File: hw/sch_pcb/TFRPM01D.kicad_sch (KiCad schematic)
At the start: 22 parts, among them J1 HEADER_1x03, J2 SM04B-GHS-TB, J3 SM04B-GHS-TB, M2 M3, U1 PCF8583, U2 SN74LVC1G14-Q1, U3 MIC5504-3.3YM5

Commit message: update action, clean repo
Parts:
- added D3: LED GREEN, LED_SMD:LED_1206_3216Metric_ReverseMount_Hole1.8x2.4mm, symbol Device:LED
- added R5: R, Resistor_SMD:R_0603_1608Metric, symbol Device:R
- C1, C4, C5, C6: footprint Mlab_R:SMD-0603 -> Capacitor_SMD:C_0603_1608Metric
- C2, C3: footprint Mlab_R:SMD-0805 -> Capacitor_SMD:C_0805_2012Metric
- D1: footprint Mlab_D:Diode-MiniMELF_Standard -> Diode_SMD:D_MiniMELF
- D2: footprint Mlab_D:LED_1206 -> LED_SMD:LED_1206_3216Metric_ReverseMount_Hole1.8x2.4mm
- R1, R2: footprint Mlab_R:SMD-0805 -> Resistor_SMD:R_0805_2012Metric
- R10, R3, R4: footprint Mlab_R:SMD-0603 -> Resistor_SMD:R_0603_1608Metric
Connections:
- net +5V: now also D3.2 (A)
- net GND: now also R5.2
- new net: D3.1 (K), R5.1

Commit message: procisteni dat
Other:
- title: TFRPM01C -> TFRPM01D
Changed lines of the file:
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@@
   (paper "A4")
   (title_block
-    (title "TFRPM01C")
-    (date "2021-04-05")
+    (title "TFRPM01D")
+    (date "2022-03-29")
     (company "ThunderFly s.r.o.")
     (comment 1 "RPM measuring device for UAVs")
     (comment 2 "Jacho  <info@thunderfly.cz>")
+    (comment 3 "roman-dvorak")
   )
   (junction (at 165.1 111.76) (diameter 1.016) (color 0 0 0 0)

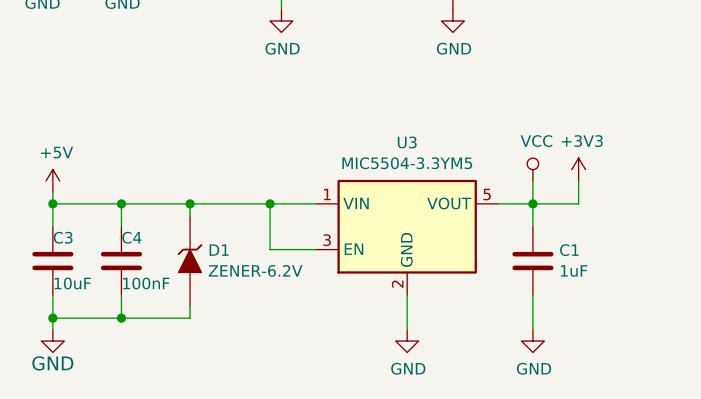
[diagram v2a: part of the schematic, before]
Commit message: Výměna pouzder LED a D zener
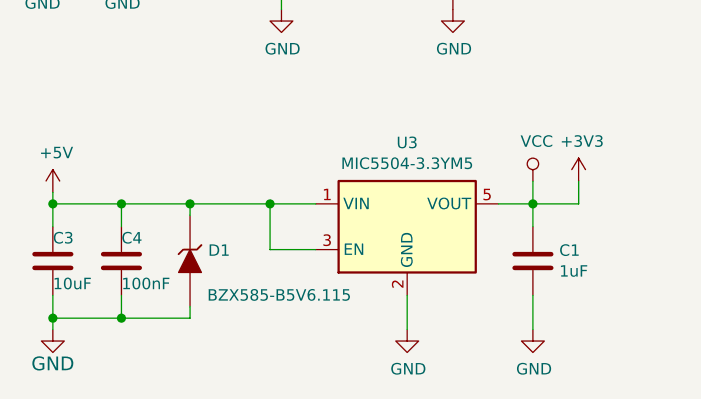
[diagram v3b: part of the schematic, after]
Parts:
- D1: value ZENER-6.2V -> BZX585-B5V6.115; footprint Diode_SMD:D_MiniMELF -> Diode_SMD:D_SOD-523; UST_ID 604b0326128750769e5b0f93 -> 60879d38128750769ee58e48
- D2, D3: footprint LED_SMD:LED_1206_3216Metric_ReverseMount_Hole1.8x2.4mm -> Mlab_D:LED_1206
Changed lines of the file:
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@@
       (effects (font (size 1.27 1.27)) (justify left))
     )
-    (property "Value" "ZENER-6.2V" (id 1) (at 45.187 176.403 90)
-      (effects (font (size 1.27 1.27)) (justify left))
-    )
-    (property "Footprint" "Diode_SMD:D_MiniMELF" (id 2) (at 43.18 175.26 0)
+    (property "Value" "BZX585-B5V6.115" (id 1) (at 45.085 179.07 90)
+      (effects (font (size 1.27 1.27)) (justify left))
+    )
+    (property "Footprint" "Diode_SMD:D_SOD-523" (id 2) (at 43.18 175.26 0)
       (effects (font (size 1.524 1.524)) hide)
     )
@@
       (effects (font (size 1.27 1.27)) hide)
     )
-    (property "UST_ID" "604b0326128750769e5b0f93" (id 5) (at 43.18 175.26 0)
+    (property "UST_ID" "60879d38128750769ee58e48" (id 5) (at 43.18 175.26 0)
       (effects (font (size 1.27 1.27)) hide)
     )
@@
     (property "Reference" "D2" (id 0) (at 103.9114 58.0136 0))
     (property "Value" "LED RED" (id 1) (at 103.9114 60.325 0))
-    (property "Footprint" "LED_SMD:LED_1206_3216Metric_ReverseMount_Hole1.8x2.4mm" (id 2) (at 104.14 63.5 0)
+    (property "Footprint" "Mlab_D:LED_1206" (id 2) (at 104.14 63.5 0)
       (effects (font (size 1.27 1.27)) hide)
     )
@@
     (property "Reference" "D3" (id 0) (at 66.9036 136.1186 0))
     (property "Value" "LED GREEN" (id 1) (at 69.215 136.1186 0))
-    (property "Footprint" "LED_SMD:LED_1206_3216Metric_ReverseMount_Hole1.8x2.4mm" (id 2) (at 72.39 135.89 0)
+    (property "Footprint" "Mlab_D:LED_1206" (id 2) (at 72.39 135.89 0)
       (effects (font (size 1.27 1.27)) hide)
     )
@@
     )
     (path "/00000000-0000-0000-0000-000059ffcb7d"
-      (reference "D1") (unit 1) (value "ZENER-6.2V") (footprint "Diode_SMD:D_MiniMELF")
+      (reference "D1") (unit 1) (value "BZX585-B5V6.115") (footprint "Diode_SMD:D_SOD-523")
     )
     (path "/00000000-0000-0000-0000-00005b1bc617"
-      (reference "D2") (unit 1) (value "LED RED") (footprint "LED_SMD:LED_1206_3216Metric_ReverseMount_Hole1.8x2.4mm")
+      (reference "D2") (unit 1) (value "LED RED") (footprint "Mlab_D:LED_1206")
     )
     (path "/158af5df-cc1b-4506-bbe6-cb7505295b5b"
-      (reference "D3") (unit 1) (value "LED GREEN") (footprint "LED_SMD:LED_1206_3216Metric_ReverseMount_Hole1.8x2.4mm")
+      (reference "D3") (unit 1) (value "LED GREEN") (footprint "Mlab_D:LED_1206")
     )
     (path "/00000000-0000-0000-0000-00005de84efb"

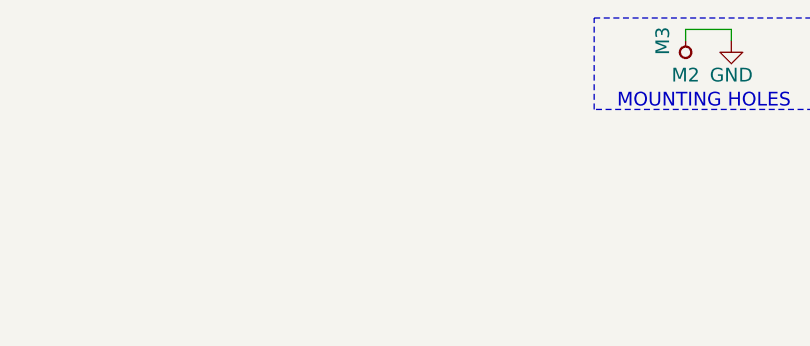
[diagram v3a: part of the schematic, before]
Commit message: Edit PCB. LED footprint. 10uF 0805 to 0603
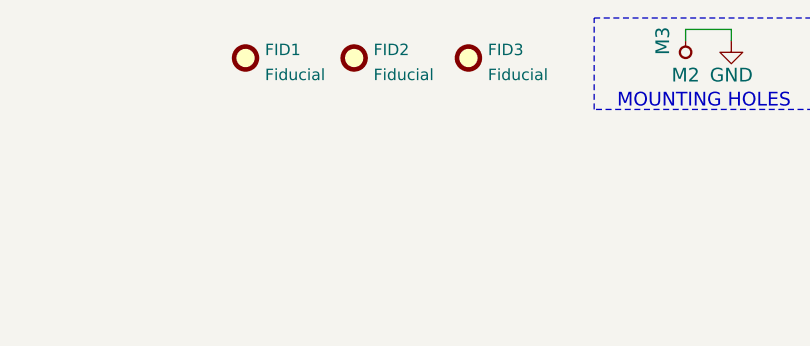
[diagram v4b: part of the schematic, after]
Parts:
- added FID1, FID2, FID3: Fiducial, symbol Mechanical:Fiducial
- C2, C3: footprint Capacitor_SMD:C_0805_2012Metric -> Capacitor_SMD:C_0603_1608Metric; UST_ID 5c70984812875079b91f8bbd -> (none)
- D2, D3: footprint Mlab_D:LED_1206 -> Mlab_D:LED_1206_2
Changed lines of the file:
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@@
       (effects (font (size 1.27 1.27)) (justify left))
     )
-    (property "Footprint" "Capacitor_SMD:C_0805_2012Metric" (id 2) (at 27.94 175.26 0)
+    (property "Footprint" "Capacitor_SMD:C_0603_1608Metric" (id 2) (at 27.94 175.26 0)
       (effects (font (size 1.524 1.524)) hide)
     )
@@
       (effects (font (size 1.27 1.27)) hide)
     )
-    (property "UST_ID" "5c70984812875079b91f8bbd" (id 5) (at 27.94 175.26 0)
+    (property "UST_ID" "" (id 5) (at 27.94 175.26 0)
       (effects (font (size 1.27 1.27)) hide)
     )
@@
     (property "Reference" "D2" (id 0) (at 103.9114 58.0136 0))
     (property "Value" "LED RED" (id 1) (at 103.9114 60.325 0))
-    (property "Footprint" "Mlab_D:LED_1206" (id 2) (at 104.14 63.5 0)
+    (property "Footprint" "Mlab_D:LED_1206_2" (id 2) (at 104.14 63.5 0)
       (effects (font (size 1.27 1.27)) hide)
     )
@@
       (effects (font (size 1.27 1.27)) (justify left))
     )
-    (property "Footprint" "Capacitor_SMD:C_0805_2012Metric" (id 2) (at 149.5552 74.93 0)
+    (property "Footprint" "Capacitor_SMD:C_0603_1608Metric" (id 2) (at 149.5552 74.93 0)
       (effects (font (size 1.27 1.27)) hide)
     )
@@
       (effects (font (size 1.27 1.27)) hide)
     )
-    (property "UST_ID" "5c70984812875079b91f8bbd" (id 5) (at 148.59 71.12 0)
+    (property "UST_ID" "" (id 5) (at 148.59 71.12 0)
       (effects (font (size 1.27 1.27)) hide)
     )
@@
     (property "Reference" "D3" (id 0) (at 66.9036 136.1186 0))
     (property "Value" "LED GREEN" (id 1) (at 69.215 136.1186 0))
-    (property "Footprint" "Mlab_D:LED_1206" (id 2) (at 72.39 135.89 0)
+    (property "Footprint" "Mlab_D:LED_1206_2" (id 2) (at 72.39 135.89 0)
       (effects (font (size 1.27 1.27)) hide)
     )
@@
     (pin "1")
   )
+  (symbol (lib_id "Mechanical:Fiducial") (at 216.535 22.225 0) (unit 1)
+    (in_bom yes) (on_board yes) (fields_autoplaced)
+    (property "Reference" "FID1" (id 0) (at 218.694 21.3165 0)
+      (effects (font (size 1.27 1.27)) (justify left))
+    )
+    (property "Value" "Fiducial" (id 1) (at 218.694 24.0916 0)
+      (effects (font (size 1.27 1.27)) (justify left))
+    )
+    (property "Footprint" "" (id 2) (at 216.535 22.225 0)
+      (effects (font (size 1.27 1.27)) hide)
+    )
+    (property "Datasheet" "~" (id 3) (at 216.535 22.225 0)
+      (effects (font (size 1.27 1.27)) hide)
+    )
+  )
+  (symbol (lib_id "Mechanical:Fiducial") (at 228.6 22.225 0) (unit 1)
+    (in_bom yes) (on_board yes) (fields_autoplaced)
+    (property "Reference" "FID2" (id 0) (at 230.759 21.3165 0)
+      (effects (font (size 1.27 1.27)) (justify left))
+    )
+    (property "Value" "Fiducial" (id 1) (at 230.759 24.0916 0)
+      (effects (font (size 1.27 1.27)) (justify left))
+    )
+    (property "Footprint" "" (id 2) (at 228.6 22.225 0)
+      (effects (font (size 1.27 1.27)) hide)
+    )
+    (property "Datasheet" "~" (id 3) (at 228.6 22.225 0)
+      (effects (font (size 1.27 1.27)) hide)
+    )
+  )
   (symbol (lib_id "power:+5V") (at 72.39 132.08 0) (unit 1)
     (in_bom yes) (on_board yes)
@@
     (pin "2")
     (pin "3")
+  )
+  (symbol (lib_id "Mechanical:Fiducial") (at 241.3 22.225 0) (unit 1)
+    (in_bom yes) (on_board yes) (fields_autoplaced)
+    (property "Reference" "FID3" (id 0) (at 243.459 21.3165 0)
+      (effects (font (size 1.27 1.27)) (justify left))
+    )
+    (property "Value" "Fiducial" (id 1) (at 243.459 24.0916 0)
+      (effects (font (size 1.27 1.27)) (justify left))
+    )
+    (property "Footprint" "" (id 2) (at 241.3 22.225 0)
+      (effects (font (size 1.27 1.27)) hide)
+    )
+    (property "Datasheet" "~" (id 3) (at 241.3 22.225 0)
+      (effects (font (size 1.27 1.27)) hide)
+    )
   )
   (sheet_instances
@@
     )
     (path "/00000000-0000-0000-0000-00005de9100e"
-      (reference "C2") (unit 1) (value "10uF") (footprint "Capacitor_SMD:C_0805_2012Metric")
+      (reference "C2") (unit 1) (value "10uF") (footprint "Capacitor_SMD:C_0603_1608Metric")
     )
     (path "/00000000-0000-0000-0000-000059ffc6a8"
-      (reference "C3") (unit 1) (value "10uF") (footprint "Capacitor_SMD:C_0805_2012Metric")
+      (reference "C3") (unit 1) (value "10uF") (footprint "Capacitor_SMD:C_0603_1608Metric")
     )
     (path "/00000000-0000-0000-0000-00005562302c"
@@
     )
     (path "/00000000-0000-0000-0000-00005b1bc617"
-      (reference "D2") (unit 1) (value "LED RED") (footprint "Mlab_D:LED_1206")
+      (reference "D2") (unit 1) (value "LED RED") (footprint "Mlab_D:LED_1206_2")
     )
     (path "/158af5df-cc1b-4506-bbe6-cb7505295b5b"
-      (reference "D3") (unit 1) (value "LED GREEN") (footprint "Mlab_D:LED_1206")
+      (reference "D3") (unit 1) (value "LED GREEN") (footprint "Mlab_D:LED_1206_2")
+    )
+    (path "/457f929f-17ed-4eee-8eba-3af909e8c516"
+      (reference "FID1") (unit 1) (value "Fiducial") (footprint "")
+    )
+    (path "/5552a350-225a-4c3c-8643-df2be6c7b9a2"
+      (reference "FID2") (unit 1) (value "Fiducial") (footprint "")
+    )
+    (path "/80ac0b57-0388-409c-bf8b-2ee44690ae03"
+      (reference "FID3") (unit 1) (value "Fiducial") (footprint "")
     )
     (path "/00000000-0000-0000-0000-00005de84efb"

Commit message: Edit
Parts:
- FID1, FID2, FID3: footprint (none) -> Fiducial:Fiducial_0.5mm_Mask1.5mm
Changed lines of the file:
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@@
       (effects (font (size 1.27 1.27)) (justify left))
     )
-    (property "Footprint" "" (id 2) (at 216.535 22.225 0)
+    (property "Footprint" "Fiducial:Fiducial_0.5mm_Mask1.5mm" (id 2) (at 216.535 22.225 0)
       (effects (font (size 1.27 1.27)) hide)
     )
@@
       (effects (font (size 1.27 1.27)) (justify left))
     )
-    (property "Footprint" "" (id 2) (at 228.6 22.225 0)
+    (property "Footprint" "Fiducial:Fiducial_0.5mm_Mask1.5mm" (id 2) (at 228.6 22.225 0)
       (effects (font (size 1.27 1.27)) hide)
     )
@@
       (effects (font (size 1.27 1.27)) (justify left))
     )
-    (property "Footprint" "" (id 2) (at 241.3 22.225 0)
+    (property "Footprint" "Fiducial:Fiducial_0.5mm_Mask1.5mm" (id 2) (at 241.3 22.225 0)
       (effects (font (size 1.27 1.27)) hide)
     )
@@
     )
     (path "/457f929f-17ed-4eee-8eba-3af909e8c516"
-      (reference "FID1") (unit 1) (value "Fiducial") (footprint "")
+      (reference "FID1") (unit 1) (value "Fiducial") (footprint "Fiducial:Fiducial_0.5mm_Mask1.5mm")
     )
     (path "/5552a350-225a-4c3c-8643-df2be6c7b9a2"
-      (reference "FID2") (unit 1) (value "Fiducial") (footprint "")
+      (reference "FID2") (unit 1) (value "Fiducial") (footprint "Fiducial:Fiducial_0.5mm_Mask1.5mm")
     )
     (path "/80ac0b57-0388-409c-bf8b-2ee44690ae03"
-      (reference "FID3") (unit 1) (value "Fiducial") (footprint "")
+      (reference "FID3") (unit 1) (value "Fiducial") (footprint "Fiducial:Fiducial_0.5mm_Mask1.5mm")
     )
     (path "/00000000-0000-0000-0000-00005de84efb"

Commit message: Edit
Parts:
- added G1: LOGO, MLAB_LOGA:TF, symbol MLAB_TF_LOGO:LOGO
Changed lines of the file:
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@@
+    )
+  )
+  (symbol (lib_id "MLAB_TF_LOGO:LOGO") (at 267.97 38.735 0) (unit 1)
+    (in_bom no) (on_board yes) (fields_autoplaced)
+    (property "Reference" "G1" (id 0) (at 282.2331 39.214 0)
+      (effects (font (size 1.27 1.27)) (justify left))
+    )
+    (property "Value" "LOGO" (id 1) (at 267.97 45.2026 0)
+      (effects (font (size 1.27 1.27)) hide)
+    )
+    (property "Footprint" "MLAB_LOGA:TF" (id 2) (at 267.97 38.735 0)
+      (effects (font (size 1.27 1.27)) hide)
+    )
+    (property "Datasheet" "" (id 3) (at 267.97 38.735 0)
+      (effects (font (size 1.27 1.27)) hide)
     )
   )
@@
       (reference "FID3") (unit 1) (value "Fiducial") (footprint "Fiducial:Fiducial_0.5mm_Mask1.5mm")
     )
+    (path "/b5ac1c53-7ad8-40c9-a438-f85c926dc816"
+      (reference "G1") (unit 1) (value "LOGO") (footprint "MLAB_LOGA:TF")
+    )
     (path "/00000000-0000-0000-0000-00005de84efb"

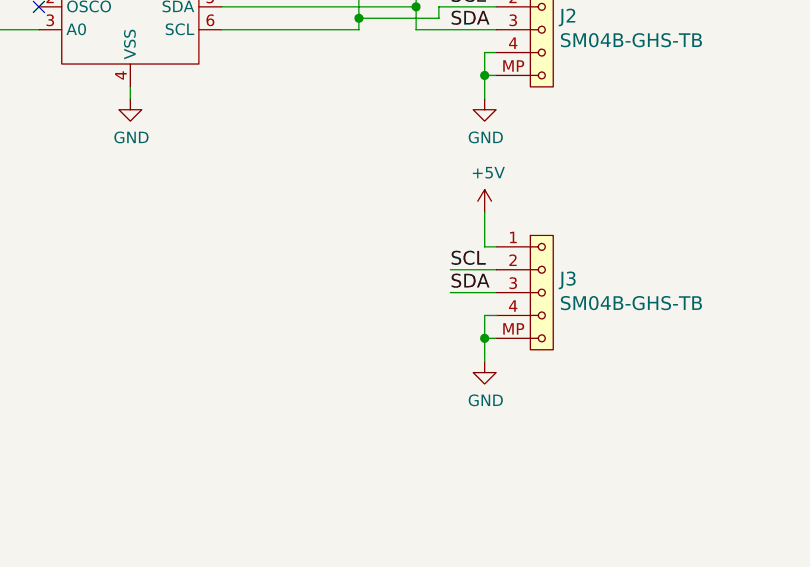
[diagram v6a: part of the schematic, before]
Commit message: Graphics and layout improvements. Net classes for default and power set.
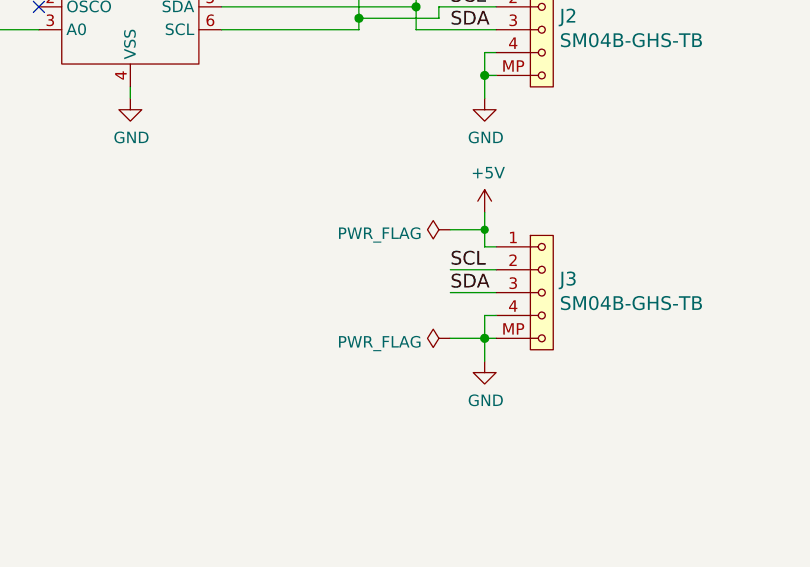
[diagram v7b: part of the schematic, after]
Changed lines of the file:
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@@
   (junction (at 52.07 168.91) (diameter 1.016) (color 0 0 0 0)
+  )
+  (junction (at 172.72 136.525) (diameter 0) (color 0 0 0 0)
   )
   (junction (at 172.72 148.59) (diameter 1.016) (color 0 0 0 0)
@@
     (stroke (width 0) (type solid) (color 0 0 0 0))
   )
-  (wire (pts (xy 172.72 134.62) (xy 172.72 138.43))
+  (wire (pts (xy 172.72 134.62) (xy 172.72 136.525))
     (stroke (width 0) (type solid) (color 0 0 0 0))
   )
@@
   (wire (pts (xy 172.72 138.43) (xy 173.99 138.43))
     (stroke (width 0) (type solid) (color 0 0 0 0))
+  )
+  (wire (pts (xy 168.91 148.59) (xy 172.72 148.59))
+    (stroke (width 0) (type default) (color 0 0 0 0))
   )
   (wire (pts (xy 43.18 180.34) (xy 43.18 181.61))
@@
     (stroke (width 0) (type solid) (color 0 0 0 0))
   )
+  (wire (pts (xy 168.91 136.525) (xy 172.72 136.525))
+    (stroke (width 0) (type default) (color 0 0 0 0))
+  )
   (wire (pts (xy 81.28 166.37) (xy 81.28 168.91))
     (stroke (width 0) (type solid) (color 0 0 0 0))
@@
   )
   (wire (pts (xy 35.56 132.08) (xy 35.56 133.35))
+    (stroke (width 0) (type solid) (color 0 0 0 0))
+  )
+  (wire (pts (xy 172.72 136.525) (xy 172.72 138.43))
     (stroke (width 0) (type solid) (color 0 0 0 0))
   )
@@
     (pin "2")
     (pin "4")
+    (pin "3")
+    (pin "5")
   )
   (symbol (lib_id "Device:LED") (at 104.14 63.5 0) (unit 1)
@@
       (effects (font (size 1.27 1.27)) hide)
     )
+    (pin "2")
+    (pin "4")
     (pin "3")
     (pin "5")
@@
     (pin "2")
   )
+  (symbol (lib_id "Power_symbols:PWR_FLAG") (at 168.91 148.59 90) (unit 1)
+    (in_bom yes) (on_board yes) (fields_autoplaced)
+    (property "Reference" "#FLG0102" (id 0) (at 167.005 148.59 0)
+      (effects (font (size 1.27 1.27)) hide)
+    )
+    (property "Value" "PWR_FLAG" (id 1) (at 165.7351 149.0238 90)
+      (effects (font (size 1.27 1.27)) (justify left))
+    )
+    (property "Footprint" "" (id 2) (at 168.91 148.59 0)
+      (effects (font (size 1.27 1.27)) hide)
+    )
+    (property "Datasheet" "~" (id 3) (at 168.91 148.59 0)
+      (effects (font (size 1.27 1.27)) hide)
+    )
+    (pin "1")
+  )
   (symbol (lib_id "Jumper:SolderJumper_3_Bridged12") (at 143.51 45.72 0) (unit 1)
     (in_bom yes) (on_board yes)
@@
     )
   )
+  (symbol (lib_id "Power_symbols:PWR_FLAG") (at 168.91 136.525 90) (unit 1)
+    (in_bom yes) (on_board yes) (fields_autoplaced)
+    (property "Reference" "#FLG0101" (id 0) (at 167.005 136.525 0)
+      (effects (font (size 1.27 1.27)) hide)
+    )
+    (property "Value" "PWR_FLAG" (id 1) (at 165.7351 136.9588 90)
+      (effects (font (size 1.27 1.27)) (justify left))
+    )
+    (property "Footprint" "" (id 2) (at 168.91 136.525 0)
+      (effects (font (size 1.27 1.27)) hide)
+    )
+    (property "Datasheet" "~" (id 3) (at 168.91 136.525 0)
+      (effects (font (size 1.27 1.27)) hide)
+    )
+    (pin "1")
+  )
   (symbol (lib_id "MLAB_TF_LOGO:LOGO") (at 267.97 38.735 0) (unit 1)
     (in_bom no) (on_board yes) (fields_autoplaced)
@@
   )
   (symbol_instances
+    (path "/9ca4be51-202c-4889-a9e8-c94e3ef56497"
+      (reference "#FLG0101") (unit 1) (value "PWR_FLAG") (footprint "")
+    )
+    (path "/243cf0cd-4978-4811-9366-3fe2caf5ac54"
+      (reference "#FLG0102") (unit 1) (value "PWR_FLAG") (footprint "")
+    )
     (path "/5a8e570e-ffc4-4fc2-953f-5233011f6a88"
       (reference "#PWR01") (unit 1) (value "+5V") (footprint "")
